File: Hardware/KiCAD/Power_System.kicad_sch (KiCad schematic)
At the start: 4 parts, among them IC7 TPS61235PRWLT, IC8 BQ24193RGER, U2 BQ297xy

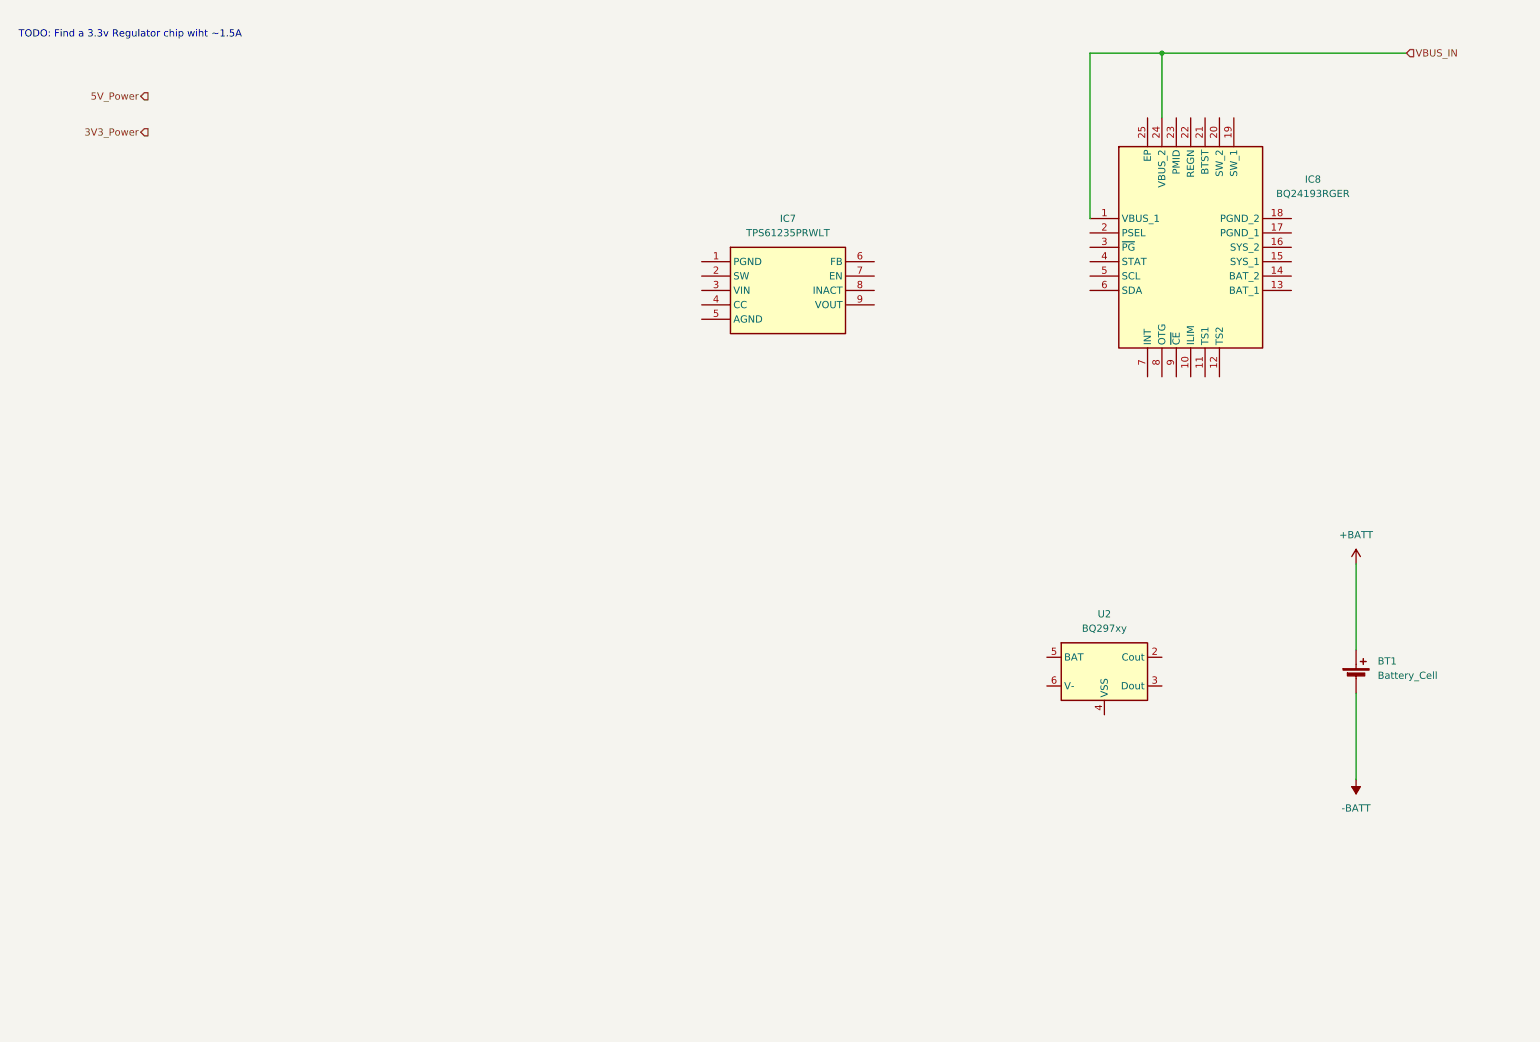
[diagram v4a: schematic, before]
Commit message: Added 3.3v converter
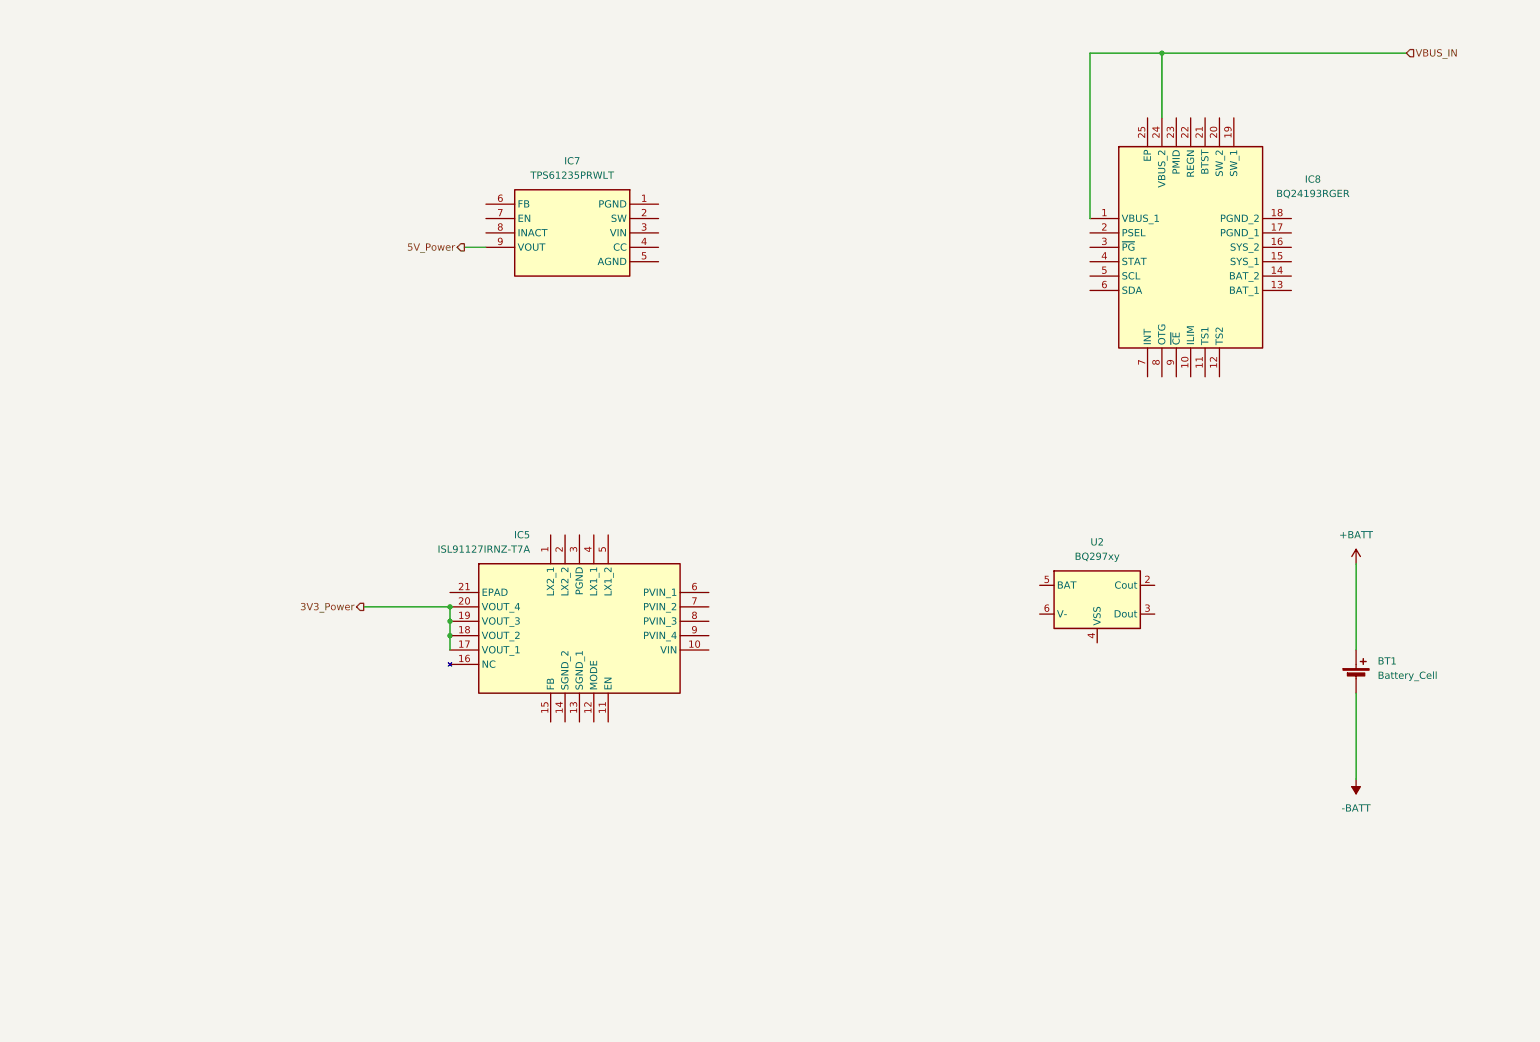
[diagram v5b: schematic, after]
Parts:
- added IC5: ISL91127IRNZ-T7A, Cobalt_Cowboy:QFN50P400X400X100-21N_ISL91127IRNZ-T7A, symbol Cobalt-Cowboy:ISL91127IRNZ-T7A
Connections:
- net 3V3_Power: now also IC5.17 (VOUT_1), IC5.18 (VOUT_2), IC5.19 (VOUT_3), IC5.20 (VOUT_4)
- net 5V_Power: now also IC7.9 (VOUT)
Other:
- note removed: "TODO: Find a 3.3v Regulator chip wiht ~1.5A"
- moved on the sheet: IC7, U2
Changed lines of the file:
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@@
 (kicad_sch (version 20230121) (generator eeschema)
   (paper "A4")
+  (junction (at 91.44 119.38) (diameter 0) (color 0 0 0 0)
+  )
   (junction (at 217.17 21.59) (diameter 0) (color 0 0 0 0)
   )
+  (junction (at 91.44 121.92) (diameter 0) (color 0 0 0 0)
+  )
+  (junction (at 91.44 124.46) (diameter 0) (color 0 0 0 0)
+  )
+  (wire (pts (xy 91.44 124.46) (xy 91.44 127))
+    (stroke (width 0) (type default))
+  )
+  (wire (pts (xy 97.79 55.88) (xy 93.98 55.88))
+    (stroke (width 0) (type default))
+  )
   (wire (pts (xy 251.46 111.76) (xy 251.46 127))
     (stroke (width 0) (type default))
@@
     (stroke (width 0) (type default))
   )
+  (wire (pts (xy 91.44 119.38) (xy 91.44 121.92))
+    (stroke (width 0) (type default))
+  )
   (wire (pts (xy 260.35 21.59) (xy 217.17 21.59))
     (stroke (width 0) (type default))
@@
     (stroke (width 0) (type default))
   )
-  (text "TODO: Find a 3.3v Regulator chip wiht ~1.5A" (at 15.24 19.05 0)
-    (effects (font (size 1.27 1.27)) (justify left bottom))
-  )
-  (hierarchical_label "3V3_Power" (shape output) (at 38.1 35.56 180) (fields_autoplaced)
+  (wire (pts (xy 76.2 119.38) (xy 91.44 119.38))
+    (stroke (width 0) (type default))
+  )
+  (wire (pts (xy 91.44 121.92) (xy 91.44 124.46))
+    (stroke (width 0) (type default))
+  )
+  (hierarchical_label "3V3_Power" (shape output) (at 76.2 119.38 180) (fields_autoplaced)
     (effects (font (size 1.27 1.27)) (justify right))
   )
@@
     (effects (font (size 1.27 1.27)) (justify left))
   )
-  (hierarchical_label "5V_Power" (shape output) (at 38.1 29.21 180) (fields_autoplaced)
+  (hierarchical_label "5V_Power" (shape output) (at 93.98 55.88 180) (fields_autoplaced)
     (effects (font (size 1.27 1.27)) (justify right))
   )
-  (symbol (lib_id "Cobalt-Cowboy:TPS61235PRWLT") (at 135.89 58.42 0) (unit 1)
+  (symbol (lib_id "Cobalt-Cowboy:TPS61235PRWLT") (at 128.27 48.26 0) (mirror y) (unit 1)
     (in_bom yes) (on_board yes) (dnp no) (fields_autoplaced)
-    (property "Reference" "IC7" (at 151.13 50.8 0)
-      (effects (font (size 1.27 1.27)))
-    )
-    (property "Value" "TPS61235PRWLT" (at 151.13 53.34 0)
-      (effects (font (size 1.27 1.27)))
-    )
-    (property "Footprint" "Cobalt_Cowboy:TPS61235PRWLT" (at 162.56 153.34 0)
-      (effects (font (size 1.27 1.27)) (justify left top) hide)
-    )
-    (property "Datasheet" "http://www.ti.com/lit/ds/symlink/tps61235p.pdf" (at 162.56 253.34 0)
-      (effects (font (size 1.27 1.27)) (justify left top) hide)
-    )
-    (property "Height" "" (at 162.56 453.34 0)
-      (effects (font (size 1.27 1.27)) (justify left top) hide)
-    )
-    (property "Manufacturer_Name" "Texas Instruments" (at 162.56 553.34 0)
-      (effects (font (size 1.27 1.27)) (justify left top) hide)
-    )
-    (property "Manufacturer_Part_Number" "TPS61235PRWLT" (at 162.56 653.34 0)
-      (effects (font (size 1.27 1.27)) (justify left top) hide)
-    )
-    (property "Mouser Part Number" "595-TPS61235PRWLT" (at 162.56 753.34 0)
-      (effects (font (size 1.27 1.27)) (justify left top) hide)
-    )
-    (property "Mouser Price/Stock" "https://www.mouser.co.uk/ProductDetail/Texas-Instruments/TPS61235PRWLT?qs=LuYMPh7GGMR%2FdWMCDntTaA%3D%3D" (at 162.56 853.34 0)
-      (effects (font (size 1.27 1.27)) (justify left top) hide)
-    )
-    (property "Arrow Part Number" "TPS61235PRWLT" (at 162.56 953.34 0)
-      (effects (font (size 1.27 1.27)) (justify left top) hide)
-    )
-    (property "Arrow Price/Stock" "https://www.arrow.com/en/products/tps61235prwlt/texas-instruments?region=nac" (at 162.56 1053.34 0)
+    (property "Reference" "IC7" (at 113.03 40.64 0)
+      (effects (font (size 1.27 1.27)))
+    )
+    (property "Value" "TPS61235PRWLT" (at 113.03 43.18 0)
+      (effects (font (size 1.27 1.27)))
+    )
+    (property "Footprint" "Cobalt_Cowboy:TPS61235PRWLT" (at 101.6 143.18 0)
+      (effects (font (size 1.27 1.27)) (justify left top) hide)
+    )
+    (property "Datasheet" "http://www.ti.com/lit/ds/symlink/tps61235p.pdf" (at 101.6 243.18 0)
+      (effects (font (size 1.27 1.27)) (justify left top) hide)
+    )
+    (property "Height" "" (at 101.6 443.18 0)
+      (effects (font (size 1.27 1.27)) (justify left top) hide)
+    )
+    (property "Manufacturer_Name" "Texas Instruments" (at 101.6 543.18 0)
+      (effects (font (size 1.27 1.27)) (justify left top) hide)
+    )
+    (property "Manufacturer_Part_Number" "TPS61235PRWLT" (at 101.6 643.18 0)
+      (effects (font (size 1.27 1.27)) (justify left top) hide)
+    )
+    (property "Mouser Part Number" "595-TPS61235PRWLT" (at 101.6 743.18 0)
+      (effects (font (size 1.27 1.27)) (justify left top) hide)
+    )
+    (property "Mouser Price/Stock" "https://www.mouser.co.uk/ProductDetail/Texas-Instruments/TPS61235PRWLT?qs=LuYMPh7GGMR%2FdWMCDntTaA%3D%3D" (at 101.6 843.18 0)
+      (effects (font (size 1.27 1.27)) (justify left top) hide)
+    )
+    (property "Arrow Part Number" "TPS61235PRWLT" (at 101.6 943.18 0)
+      (effects (font (size 1.27 1.27)) (justify left top) hide)
+    )
+    (property "Arrow Price/Stock" "https://www.arrow.com/en/products/tps61235prwlt/texas-instruments?region=nac" (at 101.6 1043.18 0)
       (effects (font (size 1.27 1.27)) (justify left top) hide)
     )
@@
     )
   )
-  (symbol (lib_id "Battery_Management:BQ297xy") (at 207.01 130.81 0) (unit 1)
+  (symbol (lib_id "Cobalt-Cowboy:ISL91127IRNZ-T7A") (at 109.22 106.68 90) (mirror x) (unit 1)
+    (in_bom yes) (on_board yes) (dnp no)
+    (property "Reference" "IC5" (at 105.5939 106.68 90)
+      (effects (font (size 1.27 1.27)) (justify left))
+    )
+    (property "Value" "ISL91127IRNZ-T7A" (at 105.5939 109.22 90)
+      (effects (font (size 1.27 1.27)) (justify left))
+    )
+    (property "Footprint" "Cobalt_Cowboy:QFN50P400X400X100-21N_ISL91127IRNZ-T7A" (at 193.98 135.89 0)
+      (effects (font (size 1.27 1.27)) (justify left top) hide)
+    )
+    (property "Datasheet" "https://www.renesas.com/en-us/www/doc/datasheet/isl91127ir.pdf" (at 293.98 135.89 0)
+      (effects (font (size 1.27 1.27)) (justify left top) hide)
+    )
+    (property "Height" "1" (at 493.98 135.89 0)
+      (effects (font (size 1.27 1.27)) (justify left top) hide)
+    )
+    (property "Manufacturer_Name" "Renesas Electronics" (at 593.98 135.89 0)
+      (effects (font (size 1.27 1.27)) (justify left top) hide)
+    )
+    (property "Manufacturer_Part_Number" "ISL91127IRNZ-T7A" (at 693.98 135.89 0)
+      (effects (font (size 1.27 1.27)) (justify left top) hide)
+    )
+    (property "Mouser Part Number" "968-ISL91127IRNZ-T7A" (at 793.98 135.89 0)
+      (effects (font (size 1.27 1.27)) (justify left top) hide)
+    )
+    (property "Mouser Price/Stock" "https://www.mouser.co.uk/ProductDetail/Renesas-Intersil/ISL91127IRNZ-T7A?qs=MbhLeWKW1It6pBrhIpi7Yg%3D%3D" (at 893.98 135.89 0)
+      (effects (font (size 1.27 1.27)) (justify left top) hide)
+    )
+    (property "Arrow Part Number" "" (at 993.98 135.89 0)
+      (effects (font (size 1.27 1.27)) (justify left top) hide)
+    )
+    (property "Arrow Price/Stock" "" (at 1093.98 135.89 0)
+      (effects (font (size 1.27 1.27)) (justify left top) hide)
+    )
+    (pin "20")
+    (pin "17")
+    (pin "6")
+    (pin "14")
+    (pin "3")
+    (pin "13")
+    (pin "15")
+    (pin "11")
+    (pin "9")
+    (pin "18")
+    (pin "8")
+    (pin "12")
+    (pin "10")
+    (pin "1")
+    (pin "19")
+    (pin "16")
+    (pin "5")
+    (pin "7")
+    (pin "21")
+    (pin "4")
+    (pin "2")
+    (instances
+      (project "Cobalt-Cowboy"
+        (path "/60a68eb1-aa0f-414e-b03b-965ad6b52dab/f41c6f3a-9e23-419e-9eda-91d37d832739"
+          (reference "IC5") (unit 1)
+        )
+      )
+    )
+  )
+  (symbol (lib_id "Battery_Management:BQ297xy") (at 205.74 118.11 0) (unit 1)
     (in_bom yes) (on_board yes) (dnp no) (fields_autoplaced)
-    (property "Reference" "U2" (at 207.01 120.65 0)
-      (effects (font (size 1.27 1.27)))
-    )
-    (property "Value" "BQ297xy" (at 207.01 123.19 0)
-      (effects (font (size 1.27 1.27)))
-    )
-    (property "Footprint" "Package_SON:WSON-6_1.5x1.5mm_P0.5mm" (at 207.01 121.92 0)
-      (effects (font (size 1.27 1.27)) hide)
-    )
-    (property "Datasheet" "http://www.ti.com/lit/ds/symlink/bq2970.pdf" (at 200.66 125.73 0)
-      (effects (font (size 1.27 1.27)) hide)
-    )
+    (property "Reference" "U2" (at 205.74 107.95 0)
+      (effects (font (size 1.27 1.27)))
+    )
+    (property "Value" "BQ297xy" (at 205.74 110.49 0)
+      (effects (font (size 1.27 1.27)))
+    )
+    (property "Footprint" "Package_SON:WSON-6_1.5x1.5mm_P0.5mm" (at 205.74 109.22 0)
+      (effects (font (size 1.27 1.27)) hide)
+    )
+    (property "Datasheet" "http://www.ti.com/lit/ds/symlink/bq2970.pdf" (at 199.39 113.03 0)
+      (effects (font (size 1.27 1.27)) hide)
+    )

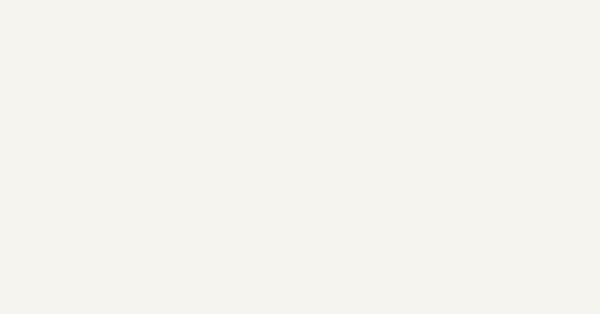
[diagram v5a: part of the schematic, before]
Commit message: Added seperate schematic for amplifier assembly
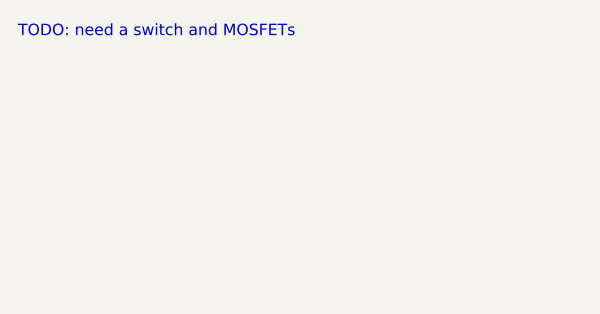
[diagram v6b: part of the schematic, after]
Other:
- note added: "TODO: need a switch and MOSFETs"
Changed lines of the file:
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@@
     (stroke (width 0) (type default))
+  )
+  (text "TODO: need a switch and MOSFETs\n" (at 13.97 16.51 0)
+    (effects (font (size 1.27 1.27)) (justify left bottom))
   )
   (hierarchical_label "3V3_Power" (shape output) (at 76.2 119.38 180) (fields_autoplaced)
